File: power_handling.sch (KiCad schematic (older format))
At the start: 50 parts, among them J1 Power In, U1 LM27762, U10 74LS32, U11 ADG734, U12 LM1085-5V, U13 ADG734, U14 ADG734, U15 LM27762, U16 ADG734, U2 ADG715, U3 LMZ34002, U4 ADG715, U5 74LS32, U6 LM1084, U7 TS12A44514, U8 TS12A44514, U9 ADG715

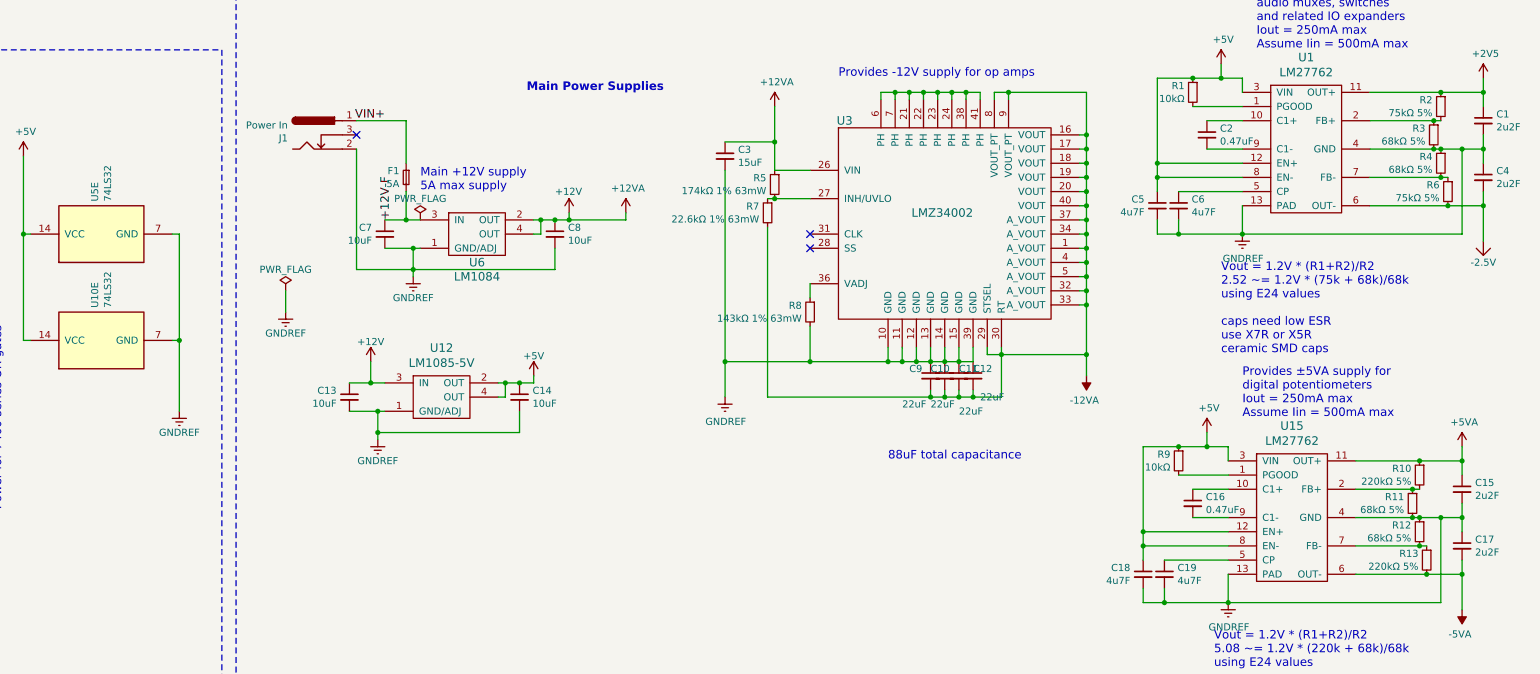
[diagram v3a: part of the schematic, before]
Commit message: Finished fixing power supply and starting pcb layout
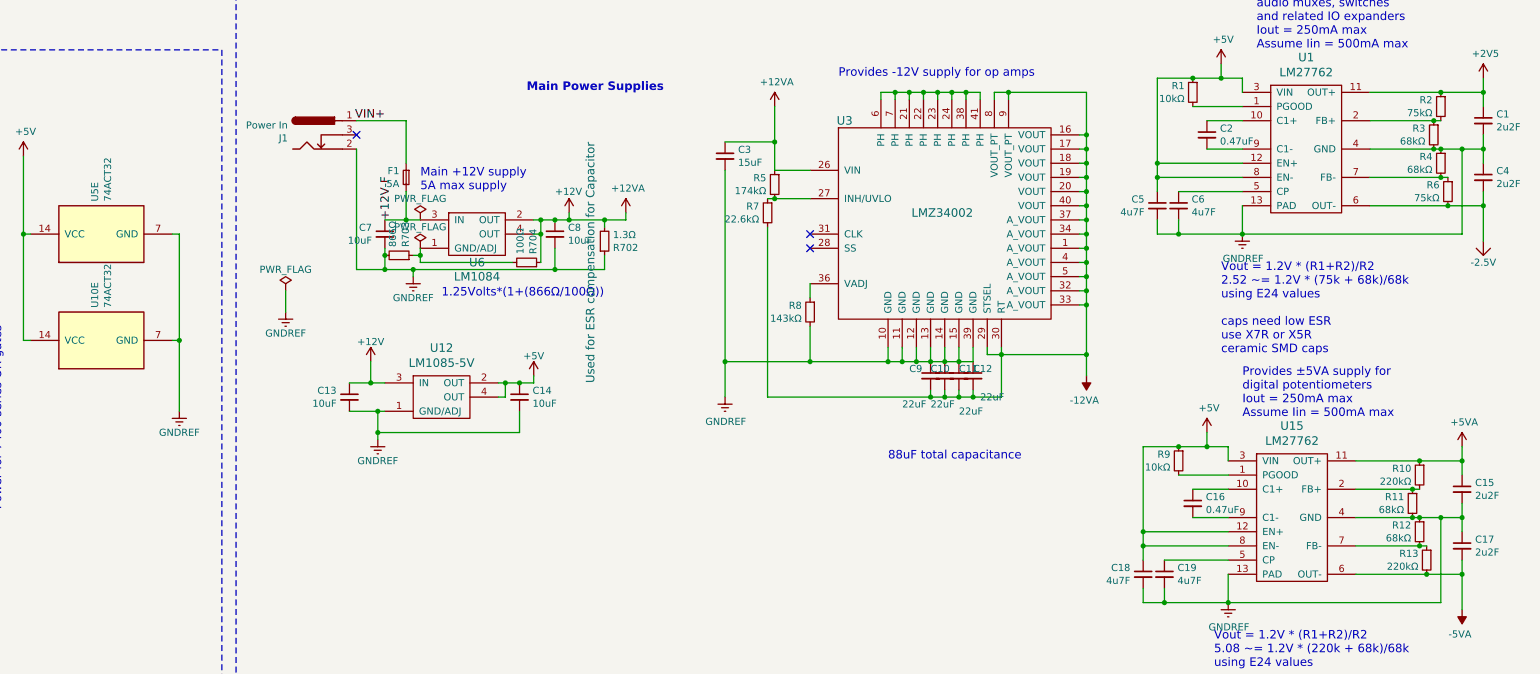
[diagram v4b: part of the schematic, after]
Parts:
- added R702: 1.3Ω, Resistor_SMD:R_0603_1608Metric_Pad0.84x1.00mm_HandSolder, symbol R_Small
- added R703: 866Ω, Resistor_SMD:R_1206_3216Metric_Pad1.24x1.80mm_HandSolder, symbol R_Small
- added R704: 100Ω, Resistor_SMD:R_1206_3216Metric_Pad1.24x1.80mm_HandSolder, symbol R_Small
- C10, C11, C12, C9: Description (none) -> Ceramic Capacitor
- C13, C14, C7: footprint Capacitor_SMD:C_0805_2012Metric_Pad1.15x1.50mm_HandSolder -> Capacitor_SMD:C_1206_3216Metric_Pad1.24x1.80mm_HandSolder; Package ID 2012 metric -> 3216 metric
- C16, C2: Characteristics (none) -> 10% -55ºC + 125ºC; Description (none) -> Ceramic Capacitor; Manufacturer (none) -> TDK; Manufacturer Part Number (none) -> CGA4J3X7R1H474K125AE
- C18, C19, C5, C6: Characteristics (none) -> 10% -55ºC +85ºC; Manufacturer (none) -> TDK; Manufacturer Part Number (none) -> CGA4J3X5R1H475K125AB
- C3: Characteristics (none) -> X5R 1.669mΩ ESR; Package ID 0805 -> 2012 metric
- C8: footprint Capacitor_SMD:C_0805_2012Metric_Pad1.15x1.50mm_HandSolder -> Capacitor_SMD:C_1206_3216Metric_Pad1.24x1.80mm_HandSolder; Characteristics (none) -> 25volts 10uF 5% X7R; Manufacturer Part Number CGA5L3X5R1H106K160AB -> C1206X106J3RACAUTO; Package ID 2012 metric -> 3216 metric
- F1: Manufacturer Part Number (none) -> 154005; Package ID 254 121 -> 254121
- R1, R9: Characteristics (none) -> 0.5% -55ºC +155ºC 100mW; Manufacturer (none) -> Vishay; Manufacturer Part Number (none) -> MCT06030D1002DP500; Package ID (none) -> 1608 metric
- R10, R13: value 220kΩ 5% -> 220kΩ; Characteristics (none) -> 0.1% -55ºC +155ºC 100mW; Description (none) -> Thin Film Resistor; Manufacturer (none) -> Vishay; Manufacturer Part Number (none) -> MCT06030D2203BP100; Package ID (none) -> 1608 metric
- R11, R12, R3, R4: value 68kΩ 5% -> 68kΩ; Characteristics (none) -> 0.1% -55ºC +155ºC 100mW; Description (none) -> Thin Film Resistor; Manufacturer (none) -> Vishay; Manufacturer Part Number (none) -> TNPW060368K0BEEA
- R2, R6: value 75kΩ 5% -> 75kΩ; Characteristics (none) -> 0.5% -55ºC +155ºC 1/8W; Description (none) -> Thin Film Resistor; Manufacturer (none) -> Vishay; Manufacturer Part Number (none) -> MCT0603MD7502DP500
- R5: value 174kΩ 1% 63mW -> 174kΩ; Characteristics (none) -> 0.1% -55ºC +155ºC 100mW; Description (none) -> Thin Film Resistor; Manufacturer Vishay-Dale -> Vishay; Manufacturer Part Number (none) -> TNPW0603174KBEEA; Notes CRCW0402174KFKED -> (none); Package ID 0402 -> 1608 metric
- R7: value 22.6kΩ 1% 63mW -> 22.6kΩ; Characteristics (none) -> 0.1% -55ºC +155ºC 100mW; Description Resistor -> Thin Film Resistor; Manufacturer Vishay-Dale -> Vishay; Manufacturer Part Number (none) -> TNPW060322K6BEEA; Notes CRCW040222K6FKED -> (none); Package ID 0402 -> 1608 metric
- R8: value 143kΩ 1% 63mW -> 143kΩ; Characteristics (none) -> 0.1% -55ºC +155ºC 100mW; Description Resistor -> Thin Film Resistor; Manufacturer Vishay-Dale -> Vishay; Manufacturer Part Number (none) -> TNPW0603143KBEEA; Notes CRCW0402143KFKED -> (none); Package ID 0402 -> 1608 metric
- U1, U15: Characteristics Vin 2.7V to 5.5V, Vout ±1.5 to 5V, ±250mA Iout, 2MHz switching frequency, -> Vin 2.7V to 5.5V, Vout ±1.5 to 5V, ±250mA Iout, 2MHz switching frequency,; Manufacturer Part Number (none) -> LM27762DSSR
- U10, U5: value 74LS32 -> 74ACT32; Description (none) -> 4x 2:1 OR Gate; Manufacturer (none) -> ON Semiconductor; Manufacturer Part Number (none) -> MC74ACT32DTR2G; Package ID (none) -> TSSOP14
- U11, U13, U14, U16: Manufacturer Part Number (none) -> ADG734BRUZ
- U12: Manufacturer Part Number (none) -> LM1085ISX-5.0/NOPB
- U2, U4, U9: Manufacturer Part Number (none) -> ADG715BRUZ; Package ID TSSOP 24 pin -> TSSOP 24 pin
- U3: Characteristics 15W Vin=4.5 to 40V, Vout = -3 to -17V, 2A out, -> 15W Vin=4.5 to 40V, Vout = -3 to -17V, 2A out,; Manufacturer Part Number (none) -> LMZ34002RKGT
- U6: footprint Package_TO_SOT_SMD:TO-263-3_TabPin4 -> SW-Texas:SOT-220-3-Horizontal-thermal-pad-NDE0003B; Manufacturer Part Number (none) -> LM1084IT-ADJ/NOPB; Notes (none) -> Adjust to 12V
- U7, U8: Manufacturer Part Number (none) -> TS12A44514PWR
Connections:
- net +12V: now also R702.2, R704.1
- net GNDREF: now also R702.1, R703.2; no longer U6.1 (GND/ADJ)
- new net: R703.1, R704.2, U6.1 (GND/ADJ)
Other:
- note added: "1.25Volts*(1+(866Ω/100Ω))"

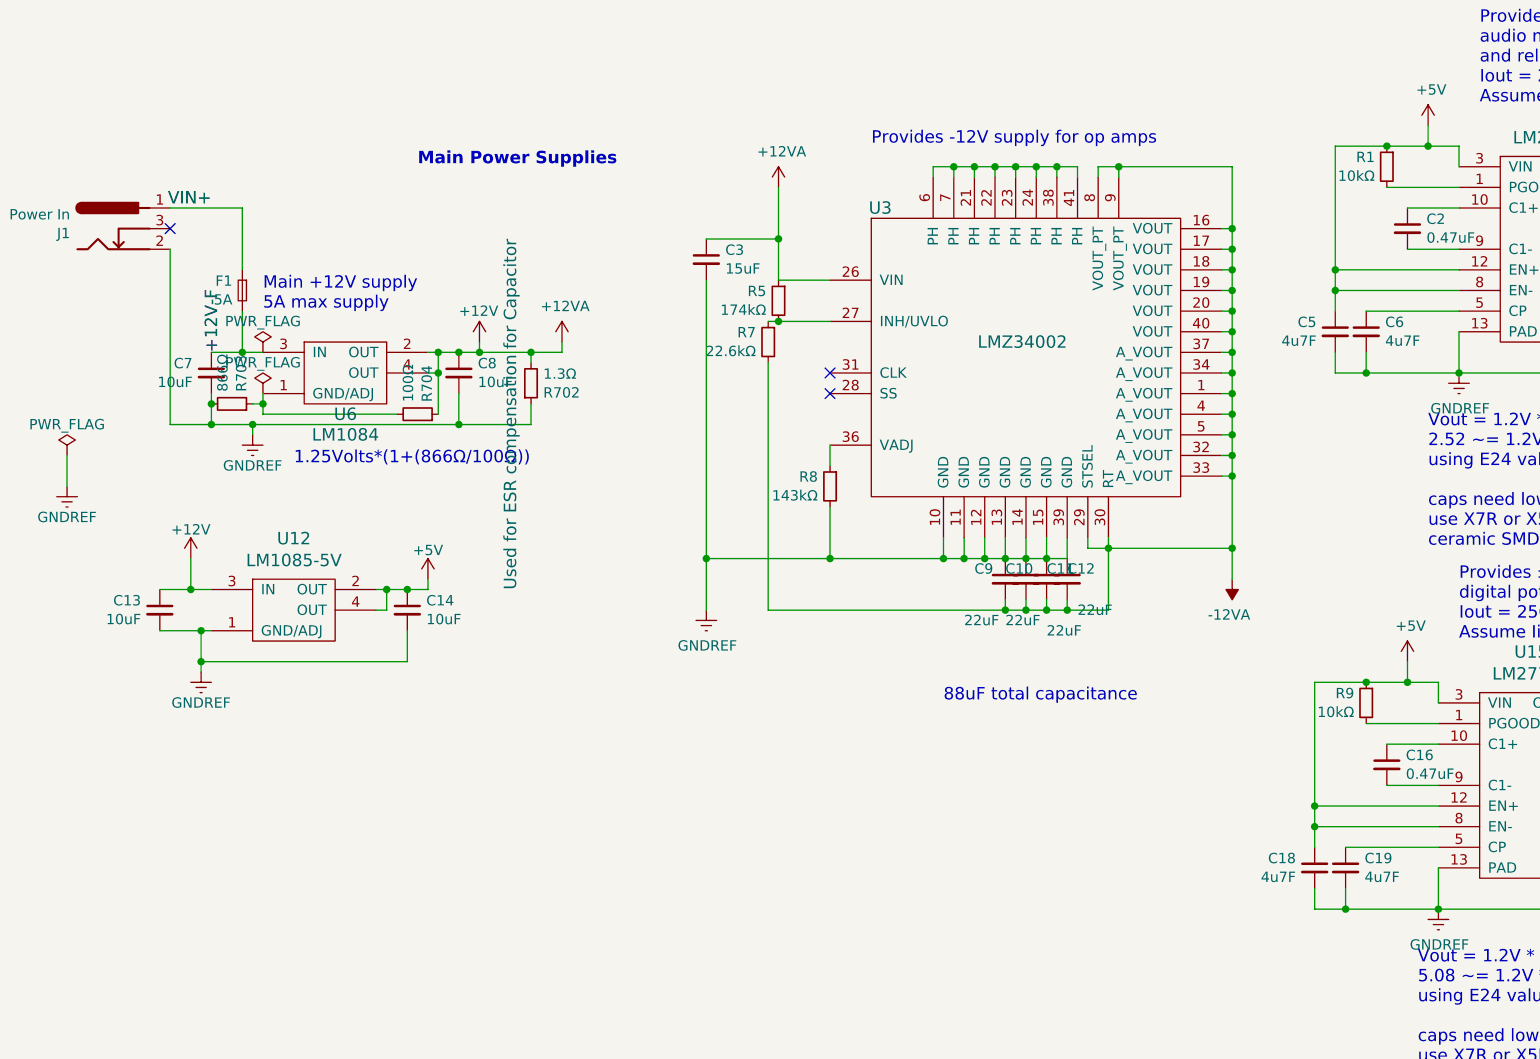
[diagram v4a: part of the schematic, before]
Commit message: More updates
- Changed 12V regulator to 3A version
- Updated readme power calculations
- Fixed which unit is used where on quad op amps
- laid out stereo distro amplifier
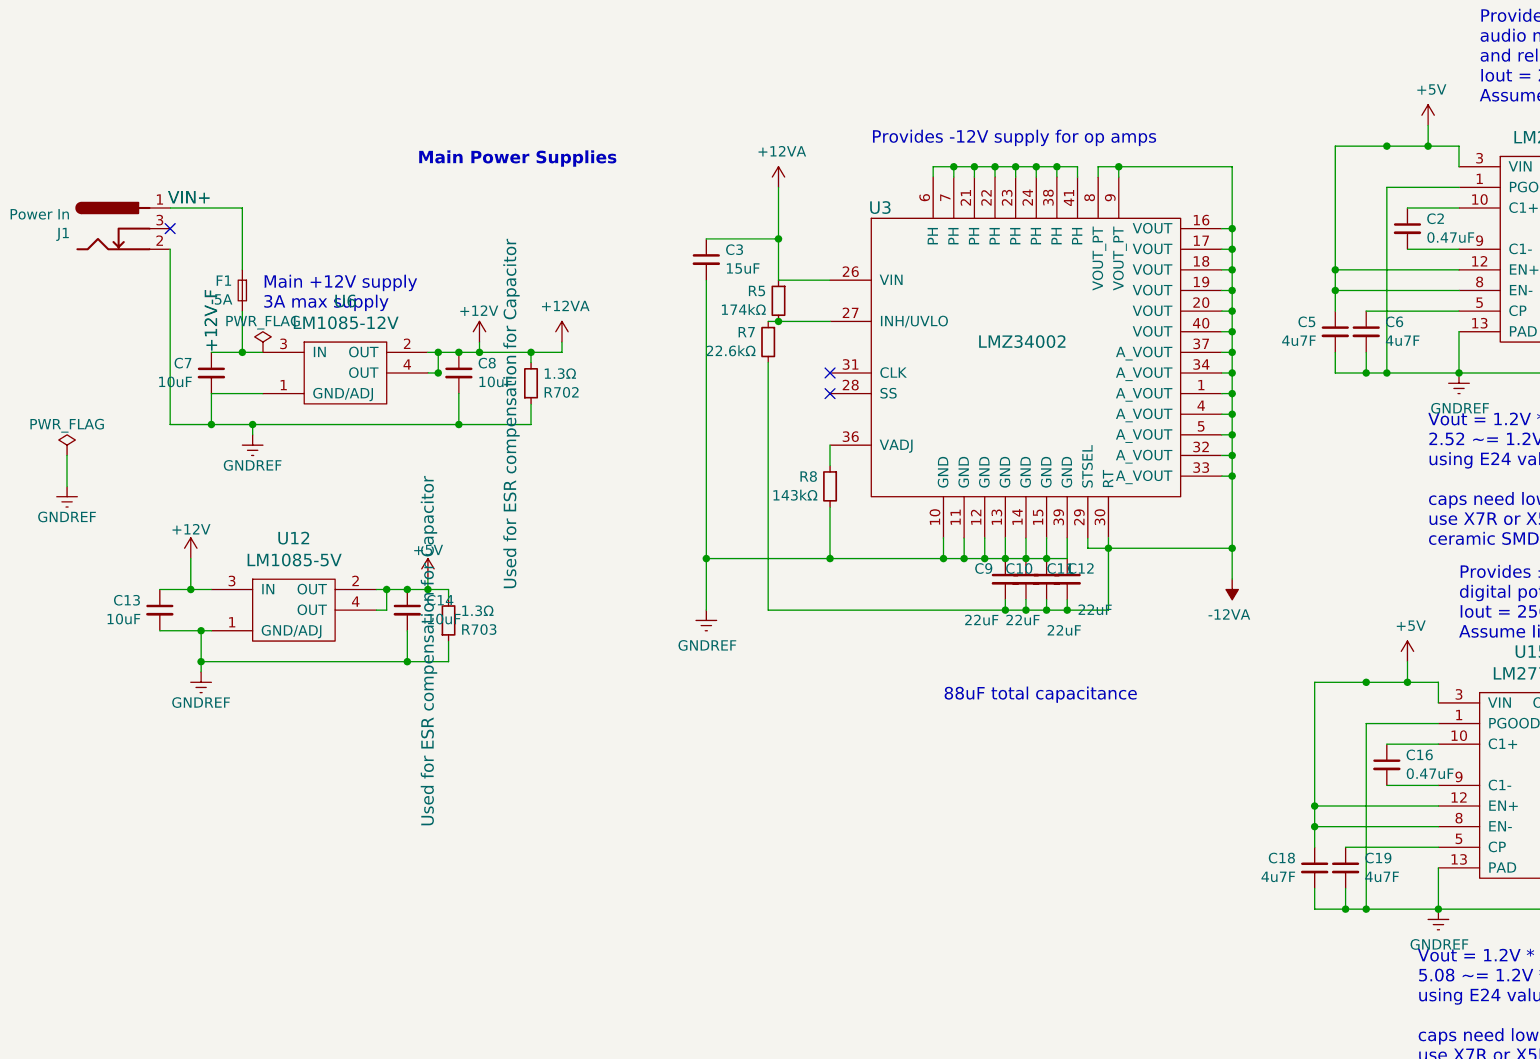
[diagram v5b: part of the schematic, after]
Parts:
- removed R1, R9: 10kΩ, Resistor_SMD:R_0603_1608Metric_Pad0.84x1.00mm_HandSolder, symbol R_Small
- removed R704: 100Ω, Resistor_SMD:R_1206_3216Metric_Pad1.24x1.80mm_HandSolder, symbol R_Small
- removed U6: LM1084, SW-Texas:SOT-220-3-Horizontal-thermal-pad-NDE0003B, symbol LM1084
- added U6: LM1085-12V, Package_TO_SOT_SMD:TO-263-3_TabPin4, symbol LM1085
- C14: Characteristics (none) -> 25volts 10uF 5% X7R; Manufacturer Part Number CGA5L3X5R1H106K160AB -> C1206X106J3RACAUTO
- R703: value 866Ω -> 1.3Ω; footprint Resistor_SMD:R_1206_3216Metric_Pad1.24x1.80mm_HandSolder -> Resistor_SMD:R_0603_1608Metric_Pad0.84x1.00mm_HandSolder; Characteristics 0.1% -55ºC +155ºC 250mW -> 0.5% -55ºC +155ºC 100mW; Manufacturer Vishay -> Yageo; Manufacturer Part Number TNPW1206866RBEEA -> RT0603DRE071R3L; Notes (none) -> Used for ESR compensation for Capacitor; Package ID 3216 metric -> 1608 metric
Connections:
- net +12V: now also U6.2 (OUT), U6.4 (OUT)
- net +12V-F: now also U6.3 (IN)
- net +5V: now also R703.2
- net GNDREF: now also R703.1, U1.1 (PGOOD), U15.1 (PGOOD), U6.1 (GND/ADJ); no longer R703.2
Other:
- note added: "Main +12V supply\n3A max supply\n"
- note removed: "1.25Volts*(1+(866Ω/100Ω))"
- note removed: "Main +12V supply\n5A max supply\n"

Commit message: Fixed 1:8 buffer amp unit mixup, placed more components
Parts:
- renumbered U5 to U17, U10 to U26
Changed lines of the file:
@@
 $EndComp
 $Comp
-L 74LS32 U10
+L 74LS32 U26
 U 5 1 59D2717B
 P 5350 3250
-F 0 "U10" H 5580 3296 50  0000 L CNN
+F 0 "U26" H 5580 3296 50  0000 L CNN
 F 1 "74ACT32" H 5580 3205 50  0000 L CNN
 F 2 "Package_SSOP:TSSOP-14_4.4x5mm_P0.65mm" H 5350 3250 50  0001 C CNN
@@
 $EndComp
 $Comp
-L 74LS32 U5
+L 74LS32 U17
 U 5 1 59D27241
 P 5350 2500
-F 0 "U5" H 5580 2546 50  0000 L CNN
+F 0 "U17" H 5580 2546 50  0000 L CNN
 F 1 "74ACT32" H 5580 2455 50  0000 L CNN
 F 2 "Package_SSOP:TSSOP-14_4.4x5mm_P0.65mm" H 5350 2500 50  0001 C CNN

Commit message: Updating to new library structure
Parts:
- C1, C10, C11, C12, C13, C14, C15, C16, C17, C18, C19, C2, C3, C4, C5, C6, C7, C8, C9: symbol C_Small -> Device:C_Small
- F1: symbol Fuse_Small -> Device:Fuse_Small
- J1: symbol Barrel_Jack -> Connector_Specialized:Barrel_Jack
- R10, R11, R12, R13, R2, R3, R4, R5, R6, R7, R702, R703, R8: symbol R_Small -> Device:R_Small
- U1, U15: symbol LM27762 -> SW-Texas:LM27762
- U11, U13, U14, U16: symbol ADG734 -> SW-Analog:ADG734
- U12, U6: symbol LM1085 -> SW-Texas:LM1085
- U17, U26: symbol 74LS32 -> Logic_74xx:74LS32
- U2, U4, U9: symbol ADG715 -> SW-Analog:ADG715
- U3: symbol LMZ34002 -> SW-Texas:LMZ34002
- U7, U8: symbol TS12A44514 -> SW-Texas:TS12A44514
